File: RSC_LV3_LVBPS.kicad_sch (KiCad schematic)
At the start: 2 parts, among them SW1 SW_SPST

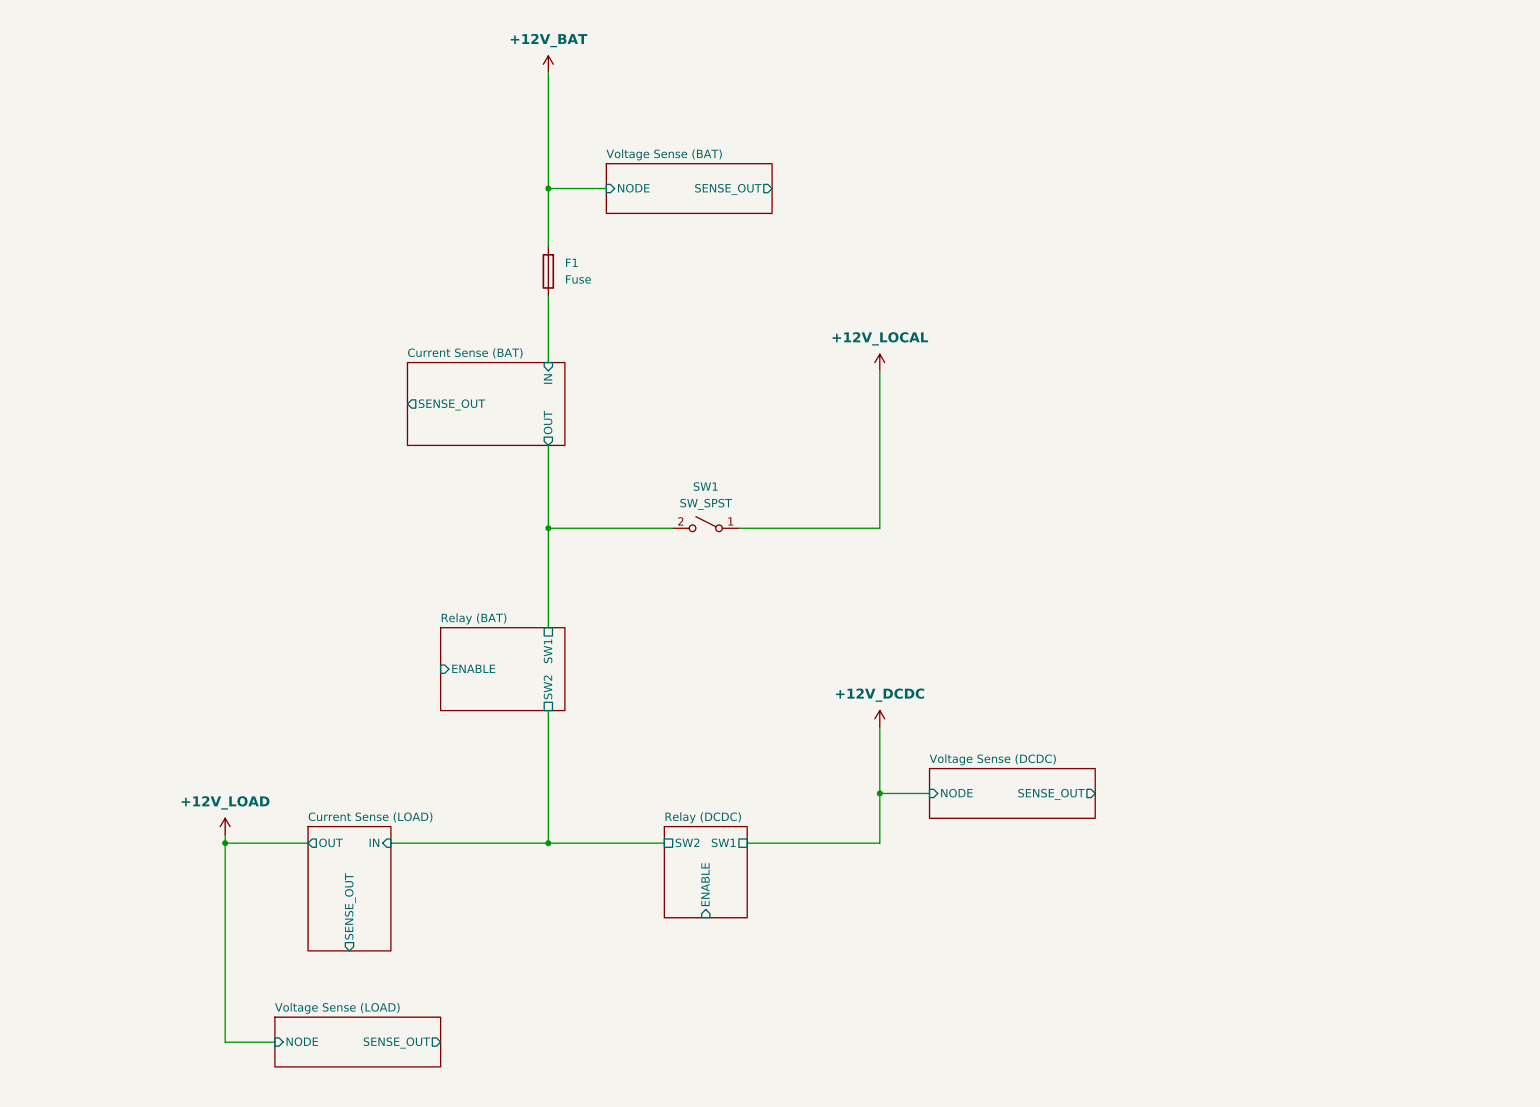
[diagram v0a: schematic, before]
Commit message: add MCU and power circuits
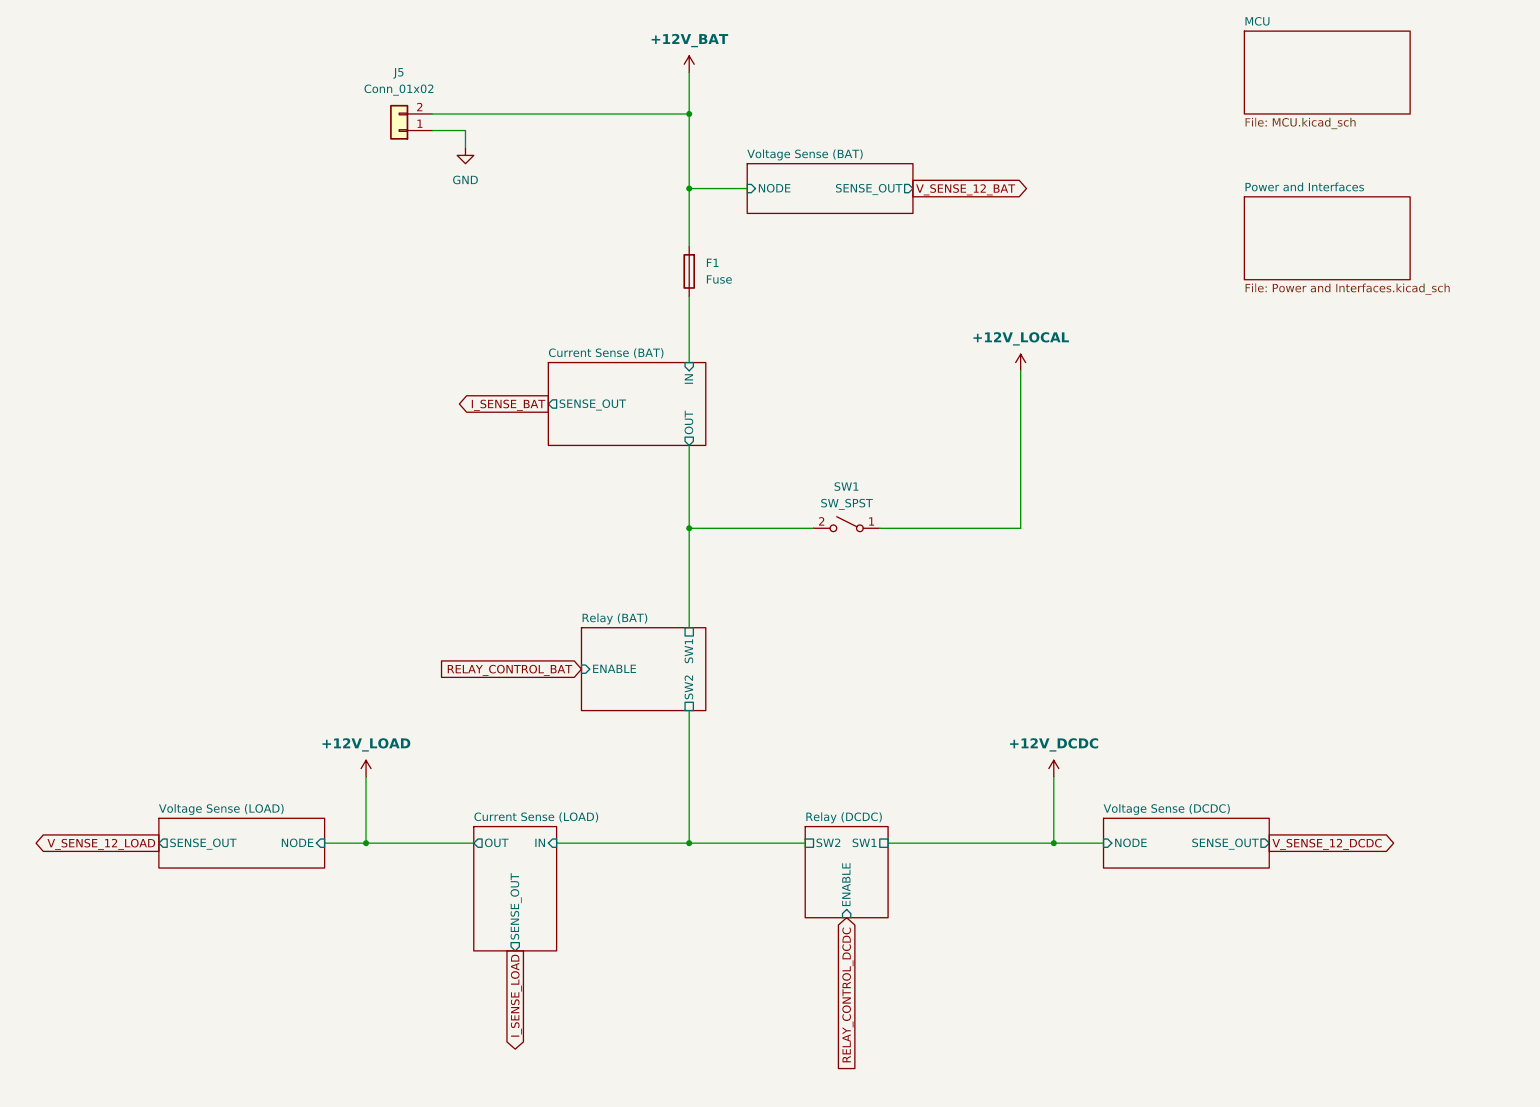
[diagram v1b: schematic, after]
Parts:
- added J5: Conn_01x02, Connector_Molex:Molex_Micro-Fit_3.0_43650-0200_1x02_P3.00mm_Horizontal, symbol Connector_Generic:Conn_01x02
- SW1: footprint (none) -> Connector_Molex:Molex_Micro-Fit_3.0_43650-0215_1x02_P3.00mm_Vertical
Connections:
- net +12V_BAT: now also J5.2 (Pin_2)
- new net GND: J5.1 (Pin_1)
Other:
- added sheet MCU (MCU.kicad_sch)
- added sheet Power and Interfaces (Power and Interfaces.kicad_sch)
- moved on the sheet: F1, SW1
